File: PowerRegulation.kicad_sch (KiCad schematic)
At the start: 35 parts, among them J10 XT60-M, J11 24V_Lockout_Key_Switch, K1 G5Q-1A DC24, Q7 BSS138, U6 TPS5430DDA, U7 XC6220B331PR-G

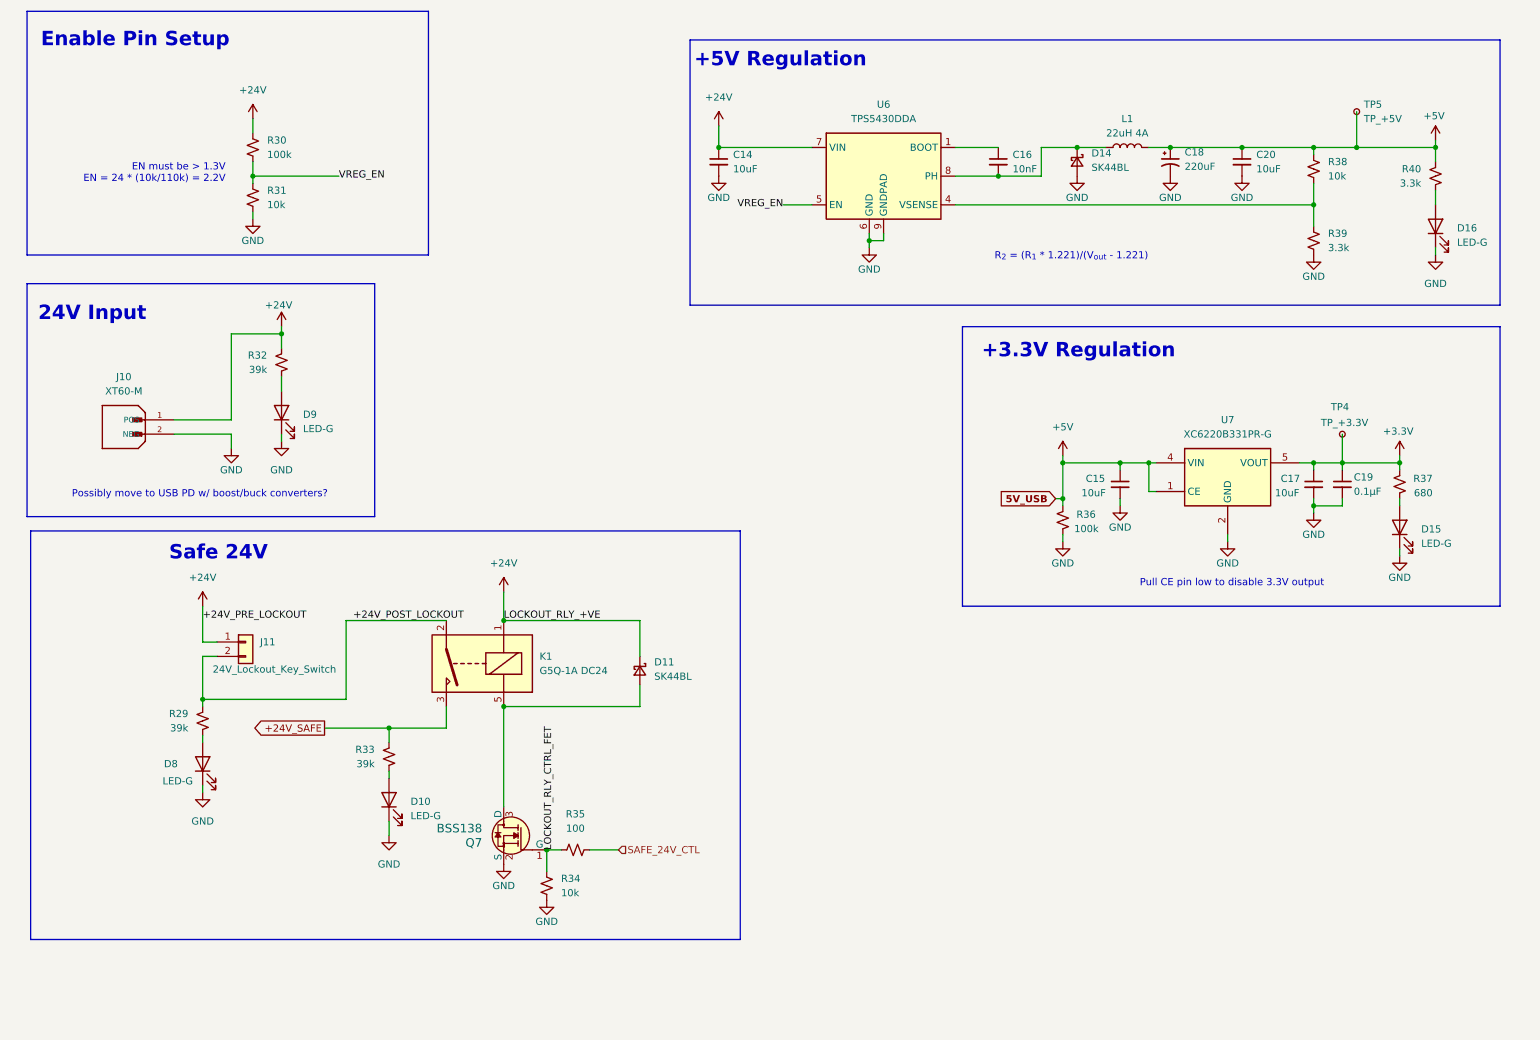
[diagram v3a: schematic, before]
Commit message: add power sequencing
add usb VBUS ORing
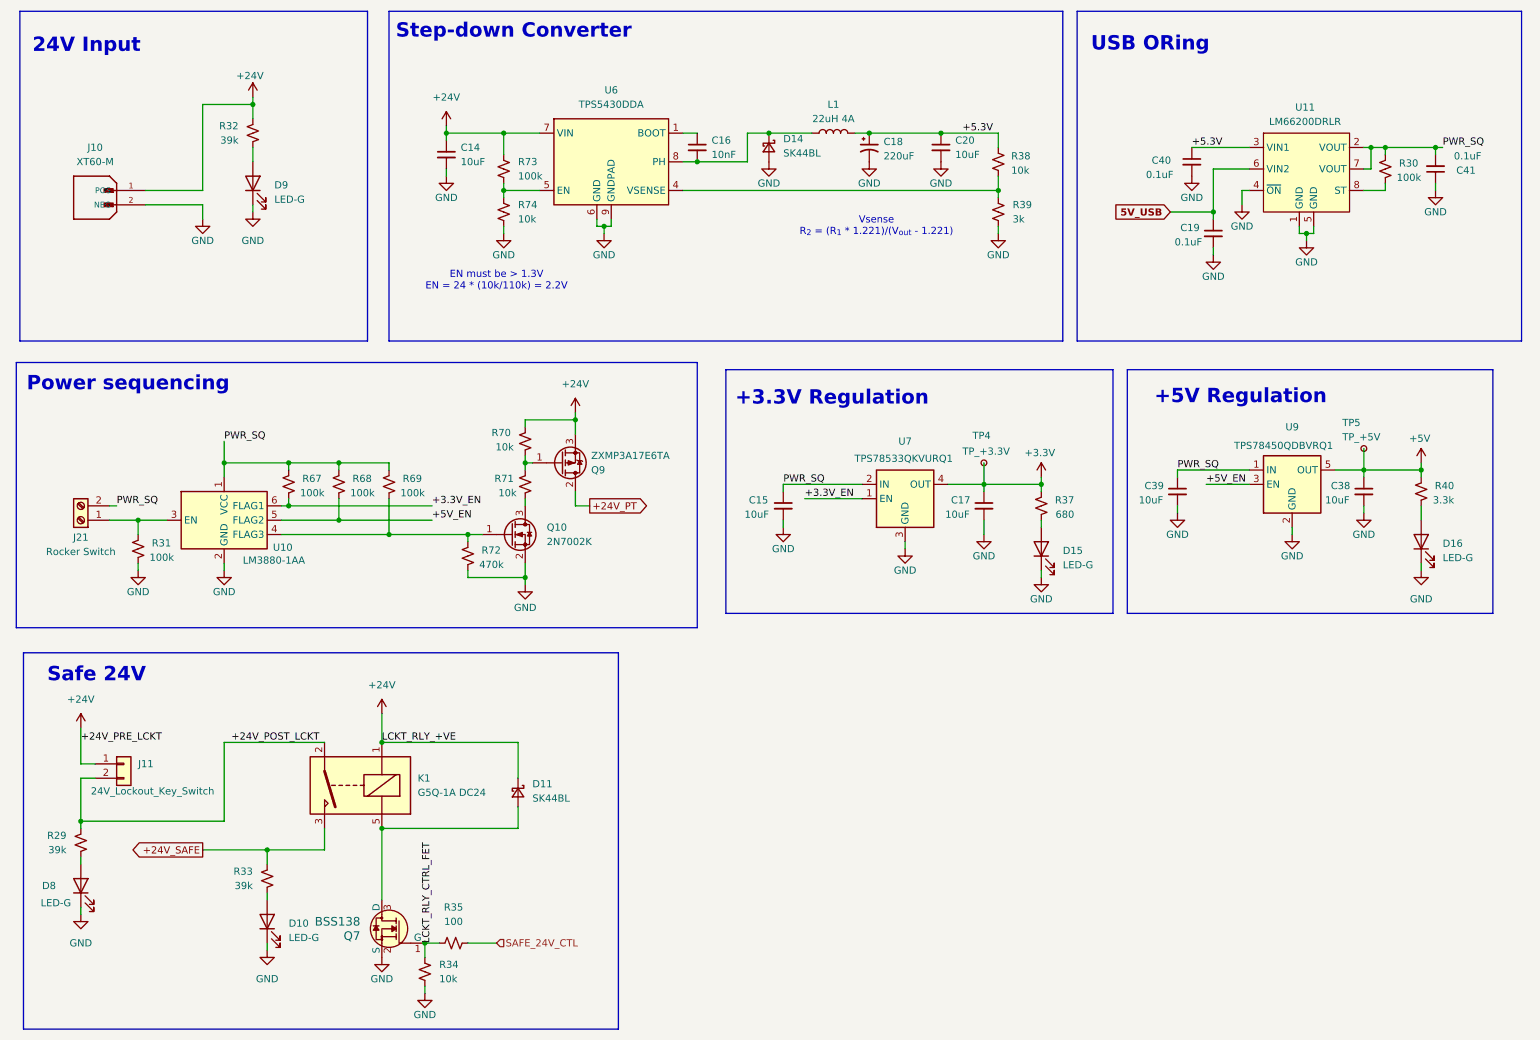
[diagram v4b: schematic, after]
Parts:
- removed R36: 100k, Resistor_SMD:R_0402_1005Metric, symbol Device:R_Small_US
- removed U7: XC6220B331PR-G, Package_TO_SOT_SMD:SOT-89-5, symbol Regulator_Linear:XC6220B331MR
- added C38, C39: 10uF, Capacitor_SMD:C_1206_3216Metric, symbol Device:C_Small
- added C40, C41: 0.1uF, Capacitor_SMD:C_1206_3216Metric, symbol Device:C_Small
- added J21: Rocker Switch, symbol Connector:Screw_Terminal_01x02
- added Q10: 2N7002K, Package_TO_SOT_SMD:SOT-23, symbol Transistor_FET:2N7002K
- added Q9: ZXMP3A17E6TA, Library:ZXMP3A17E6TA, symbol Transistor_FET:ZXMP4A16G
- added R67, R68, R69, R73: 100k, Resistor_SMD:R_0402_1005Metric, symbol Device:R_Small_US
- added R70, R71, R74: 10k, Resistor_SMD:R_0402_1005Metric, symbol Device:R_Small_US
- added R72: 470k, Resistor_SMD:R_0402_1005Metric, symbol Device:R_Small_US
- added U10: LM3880-1AA, Package_TO_SOT_SMD:SOT-23-6, symbol Power_Supervisor:LM3880
- added U11: LM66200DRLR, Package_TO_SOT_SMD:SOT-583-8, symbol LM66200DRLR:LM66200DRLR
- added U7: TPS78533QKVURQ1, Package_TO_SOT_SMD:TO-252-4, symbol Regulator_Linear:TPS78236DDC
- added U9: TPS78450QDBVRQ1, Package_TO_SOT_SMD:SOT-23-5, symbol Regulator_Linear:TPS78236DDC
- C19: value 0.1μF -> 0.1uF; footprint Capacitor_SMD:C_0402_1005Metric -> Capacitor_SMD:C_1206_3216Metric; Dielectric (none) -> X5R or X7R; LCSC C1525 -> C13585; MPN CL05B104KO5NNNC -> (none); P/N (none) -> CL31A106KBHNNNE; Voltage (none) -> 50V
- R30: LCSC C25530 -> (none); MPN 0402WGJ0104TCE -> (none)
- R31: value 10k -> 100k; LCSC C25531 -> (none); MPN 0402WGJ0103TCE -> (none)
- R39: value 3.3k -> 3k
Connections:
- net +24V: now also Q9.3 (S), R70.2, R73.1; no longer R30.1
- net +3.3V: now also U7.4 (OUT); no longer C19.1
- net +5V: now also C38.1, U9.5 (OUT); no longer C15.1, C18.1, C20.1, L1.2, R38.1
- net GND: now also R31.1, C38.2, C39.2, C40.2, C41.1, Q10.2 (S), R72.1, R74.2, U10.2 (GND), U11.1 (GND), U11.4 (~{ON}), U11.5 (GND), U7.3 (GND), U7.4 (OUT), U9.2 (GND), U9.4 (GND); no longer R31.2
- net +24V_POST_LOCKOUT renamed +24V_POST_LCKT
- net LOCKOUT_RLY_CTRL_FET renamed LCKT_RLY_CTRL_FET
- removed net VREG_EN: R30.2, R31.1, U6.5 (EN)
- new net: Q9.1 (G), R70.1, R71.2
- new net: R73.2, R74.1, U6.5 (EN)
- new net: Q10.1 (G), R69.1, R72.2, U10.4 (FLAG3)
- new net: Q10.3 (D), R71.1
- new net: R30.1, U11.8 (ST)
- new net: J21.1 (Pin_1), R31.2, U10.3 (EN)
- new net +24V_PT: Q9.2 (D)
- new net +3.3V_EN: R67.1, U10.6 (FLAG1), U7.1 (EN)
- new net +5.3V: C18.1, C20.1, C40.1, L1.2, R38.1, U11.3 (VIN1)
- new net +5V_EN: R68.1, U10.5 (FLAG2), U9.3 (EN)
- new net 5V_USB: C19.1, U11.6 (VIN2)
- new net PWR_SQ: C15.1, C39.1, C41.2, J21.2 (Pin_2), R30.2, R67.2, R68.2, R69.2, U10.1 (VCC), U11.2 (VOUT), U11.7 (VOUT), U7.2 (IN), U9.1 (IN)
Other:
- note added: "Power sequencing"
- note added: "Step-down Converter"
- note added: "USB ORing"
- note added: "Vsense R_{2} = (R_{1} * 1.221)/(V_{out} - 1.221)"
- note removed: "Enable Pin Setup"
- note removed: "Possibly move to USB PD w/ boost/buck converters?"
- note removed: "Pull CE pin low to disable 3.3V output"
- note removed: "R_{2} = (R_{1} * 1.221)/(V_{out} - 1.221)"
- moved on the sheet: C14, C15, C16, C17, C18, C20, D10, D11, D14, D15, D16, D8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
